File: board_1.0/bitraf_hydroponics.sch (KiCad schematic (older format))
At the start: 39 parts, among them P1 12V_PWR, P10 LDR, P11 ROT_BTN, P12 SWITCH_2, P13 I2C_4, P14 I2C_3, P15 I2C_2, P16 I2C_1, P17 SWITCH_3, P2 BREAKOUT_1-15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

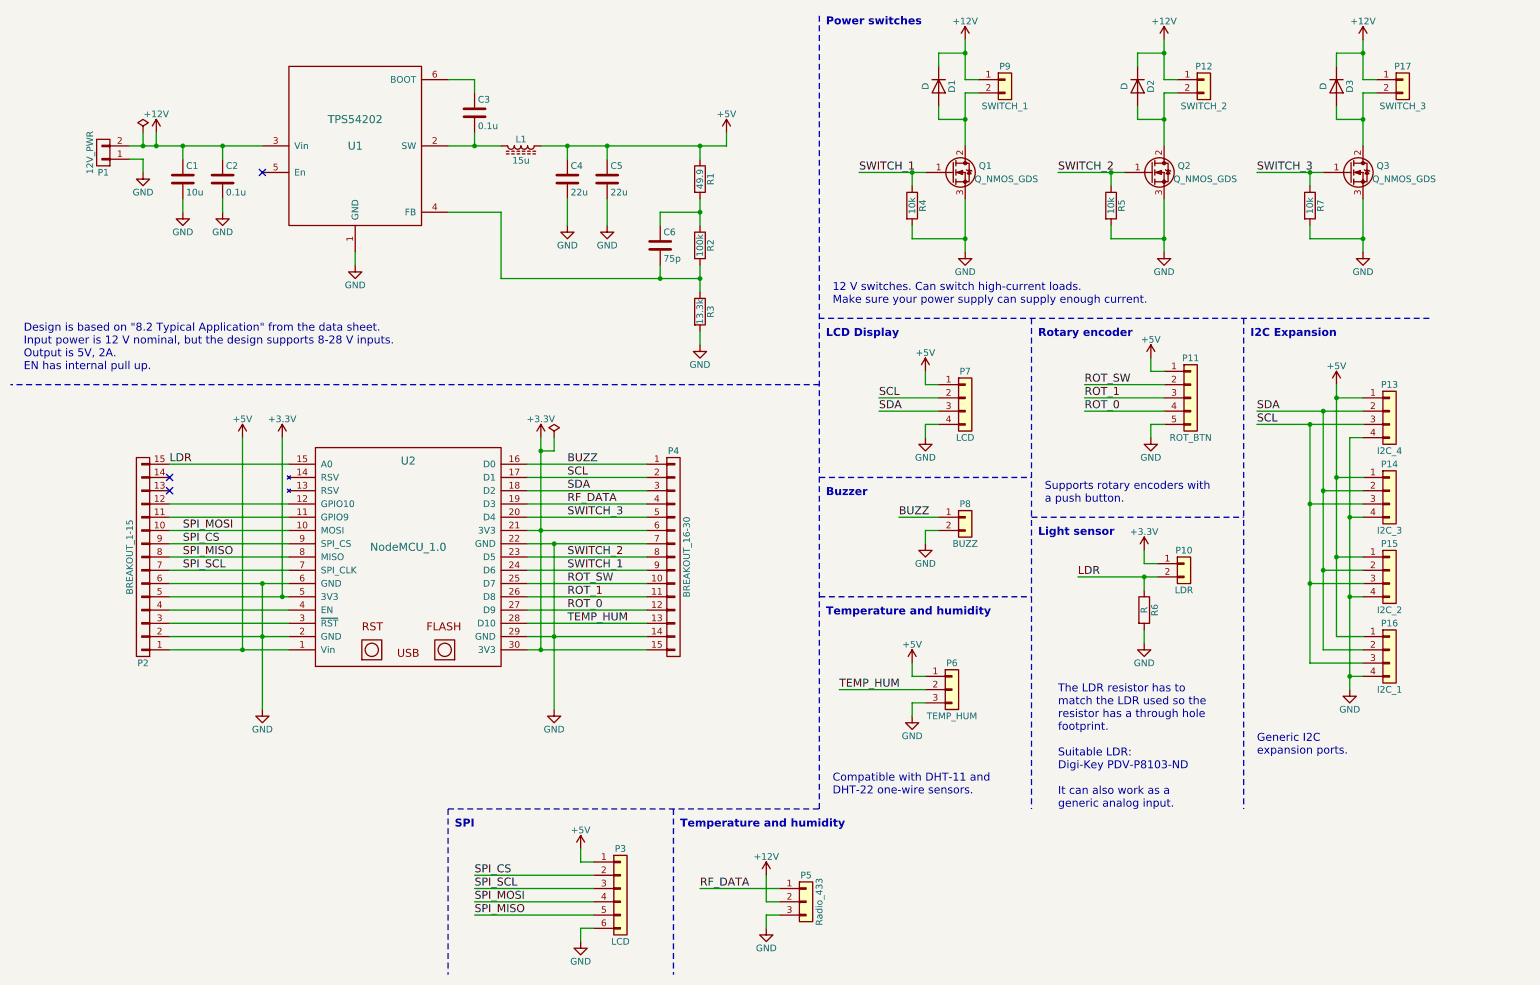
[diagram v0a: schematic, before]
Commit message: o Replacing NodeMCU with a single ESP-12F module and an LDO.   Will need an external programmer.
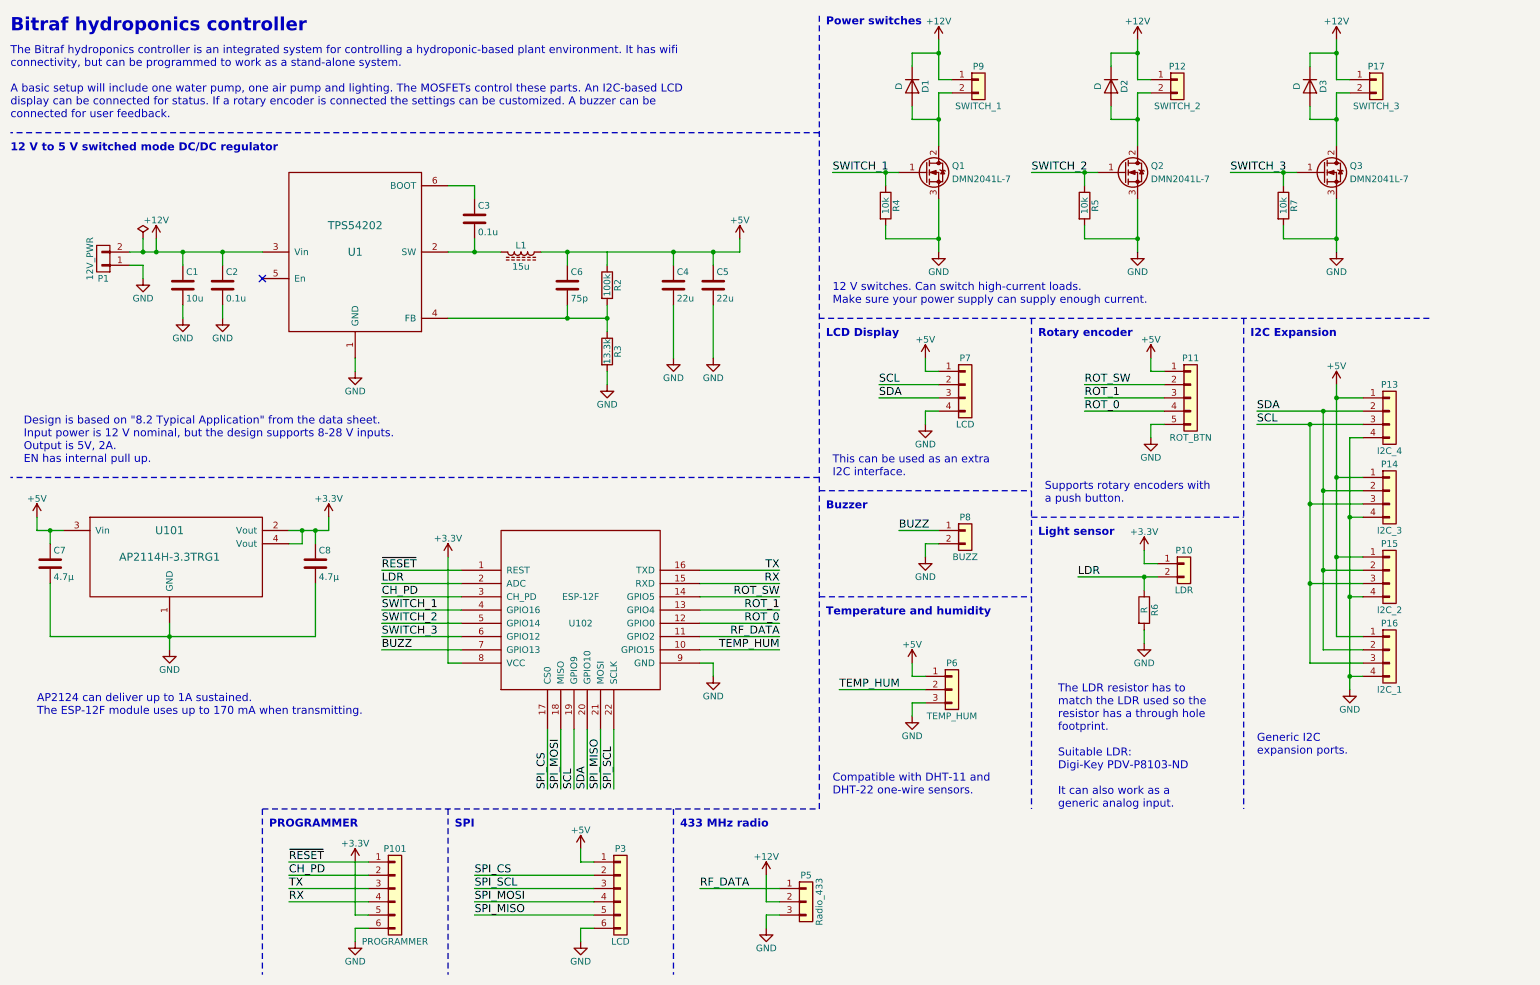
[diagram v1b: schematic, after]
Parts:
- removed P2: BREAKOUT_1-15, symbol CONN_01X15
- removed P4: BREAKOUT_16-30, symbol CONN_01X15
- removed R1: 49.9, symbol R
- removed U2: NodeMCU_1.0, symbol NodeMCU_1.0
- added C7, C8: 4.7µ, symbol C
- added P101: PROGRAMMER, symbol Conn_01x06
- added U101: AP2114H-3.3TRG1, TO_SOT_Packages_SMD:SOT-223, symbol AP2114H-3.3TRG1
- added U102: ESP-12F, ESP8266:ESP-12E, symbol ESP-12F
- Q1, Q2, Q3: value Q_NMOS_GDS -> DMN2041L-7
- U1: footprint (none) -> TO_SOT_Packages_SMD:SOT-23-6_Handsoldering
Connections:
- net +3V3: now also C8.1, P101.5 (Pin_5), U101.2 (Vout), U101.4 (Vout), U102.8 (VCC)
- net +5V: now also C6.1, C7.1, U101.3 (Vin)
- net BUZZ: now also U102.7 (GPIO13)
- net GND: now also C7.2, C8.2, P101.6 (Pin_6), U101.1 (GND), U102.9 (GND)
- net LDR: now also U102.2 (ADC)
- net RF_DATA: now also U102.11 (GPIO2)
- net ROT_0: now also U102.12 (GPIO0)
- net ROT_1: now also U102.13 (GPIO4)
- net ROT_SW: now also U102.14 (GPIO5)
- net SCL: now also U102.19 (GPIO9)
- net SDA: now also U102.20 (GPIO10)
- net SPI_CS: now also U102.17 (CS0)
- net SPI_MISO: now also U102.21 (MOSI)
- net SPI_MOSI: now also U102.18 (MISO)
- net SPI_SCL: now also U102.22 (SCLK)
- net SWITCH_1: now also U102.4 (GPIO16)
- net SWITCH_2: now also U102.5 (GPIO14)
- net SWITCH_3: now also U102.6 (GPIO12)
- net TEMP_HUM: now also U102.10 (GPIO15)
- net at R2.1: no longer C6.1
- new net CH_PD: P101.2 (Pin_2), U102.3 (CH_PD)
- new net RX: P101.4 (Pin_4), U102.15 (RXD)
- new net TX: P101.3 (Pin_3), U102.16 (TXD)
- new net ~RESET: P101.1 (Pin_1), U102.1 (REST)
- no-connect marks 3 -> 1
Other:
- note added: "12 V to 5 V switched mode DC/DC regulator"
- note added: "433 MHz radio"
- note added: "AP2124 can deliver up to 1A sustained.\nThe ESP-12F module uses up to 170 mA when transmitting."
- note added: "Bitraf hydroponics controller"
- note added: "PROGRAMMER"
- note added: "The Bitraf hydroponics controller is an integrated system for controlling a hydroponic-based plant environment. It has wifi\nconnectivity, but can be programmed to work as a stand-alone system.\n\nA basic setup will include one water pump, one air pump and lighting. The MOSFETs control these parts. An I2C-based LCD\ndisplay can be connected for status. If a rotary encoder is connected the setting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"
- note added: "This can be used as an extra\nI2C interface."
- moved on the sheet: C1, C2, C3, C4, C5, C6, D1, D2, D3, L1, P1, P12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

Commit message: o Selecting components for flyback diodes. o Adding footprints for MOSFETs. o More comments.
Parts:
- D1, D2, D3: value D -> S1MTR; footprint (none) -> Diodes_SMD:D_SMA_Handsoldering
- Q1, Q2, Q3: footprint (none) -> TO_SOT_Packages_SMD:SOT-23
- renumbered U101 to U2, U102 to U3
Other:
- note added: "Flyback diodes are "fast rectifier diodes" for inductive loads. DC Reverse Vr(max) is 1000 V,\nIo is 1 A. The MOSFETs have Vdss = 20 V, Rds(on) = 26 mΩ @ 3.3 V, Id = 6.4 A.\n"
- note removed: "12 V switches. Can switch high-current loads.\nMake sure your power supply can supply enough current."
- moved on the sheet: Q1, Q2, Q3, R4, R5, R7

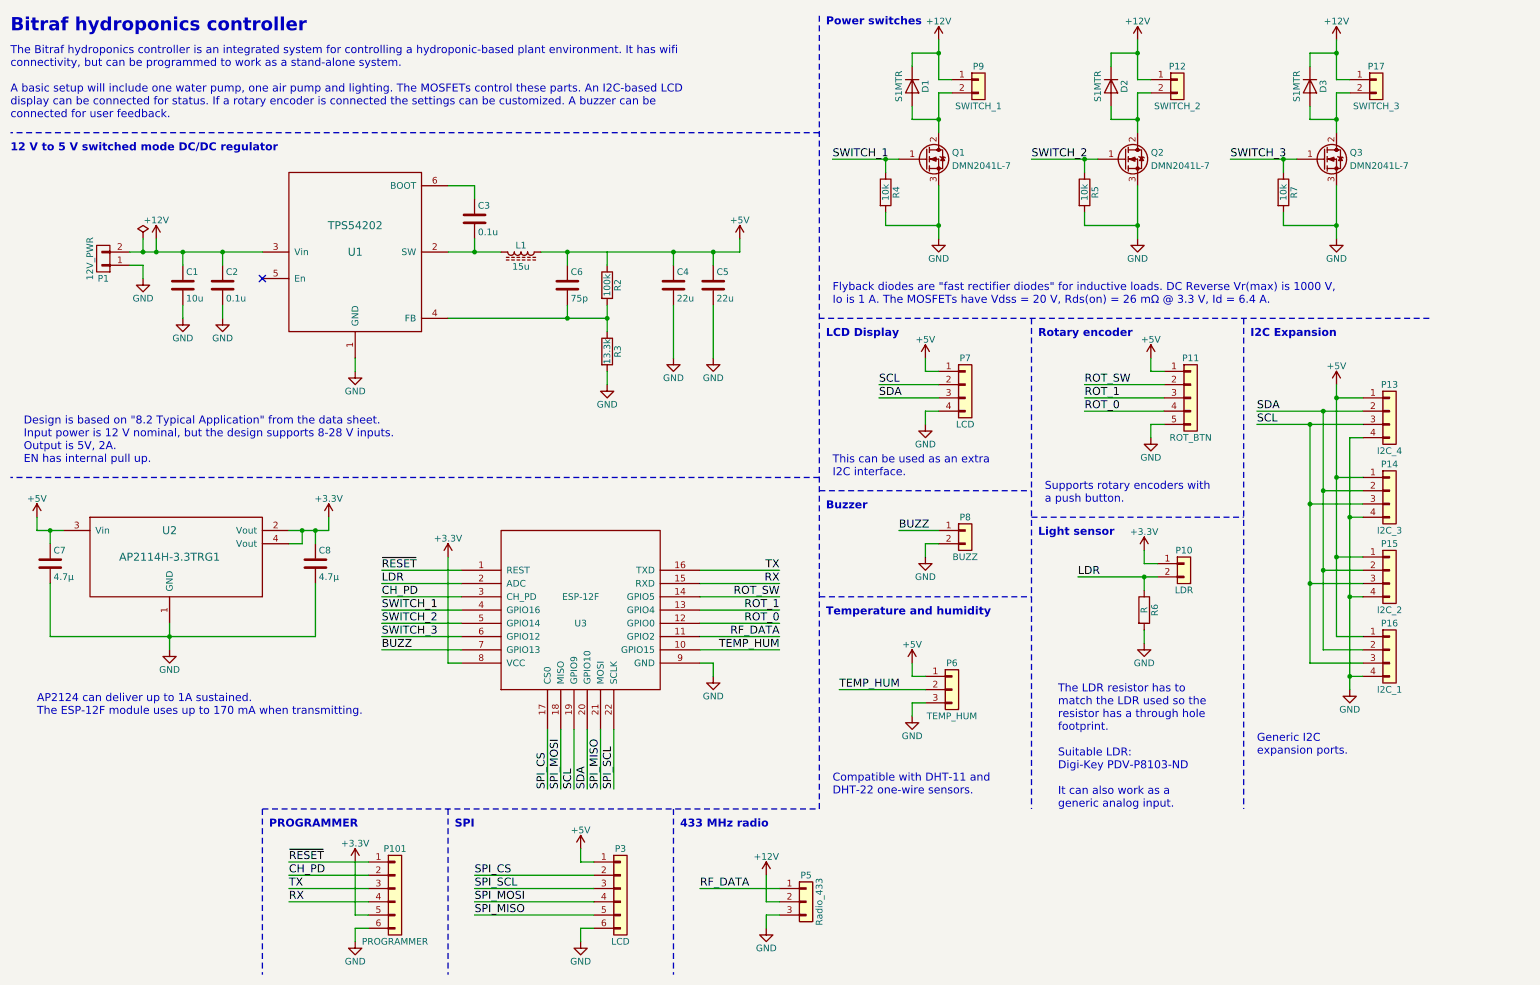
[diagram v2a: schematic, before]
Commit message: o Selecting the rest of the footprints. Using 0805 as default SMD size to make it makerspace friendly. o Some more nitpicking.
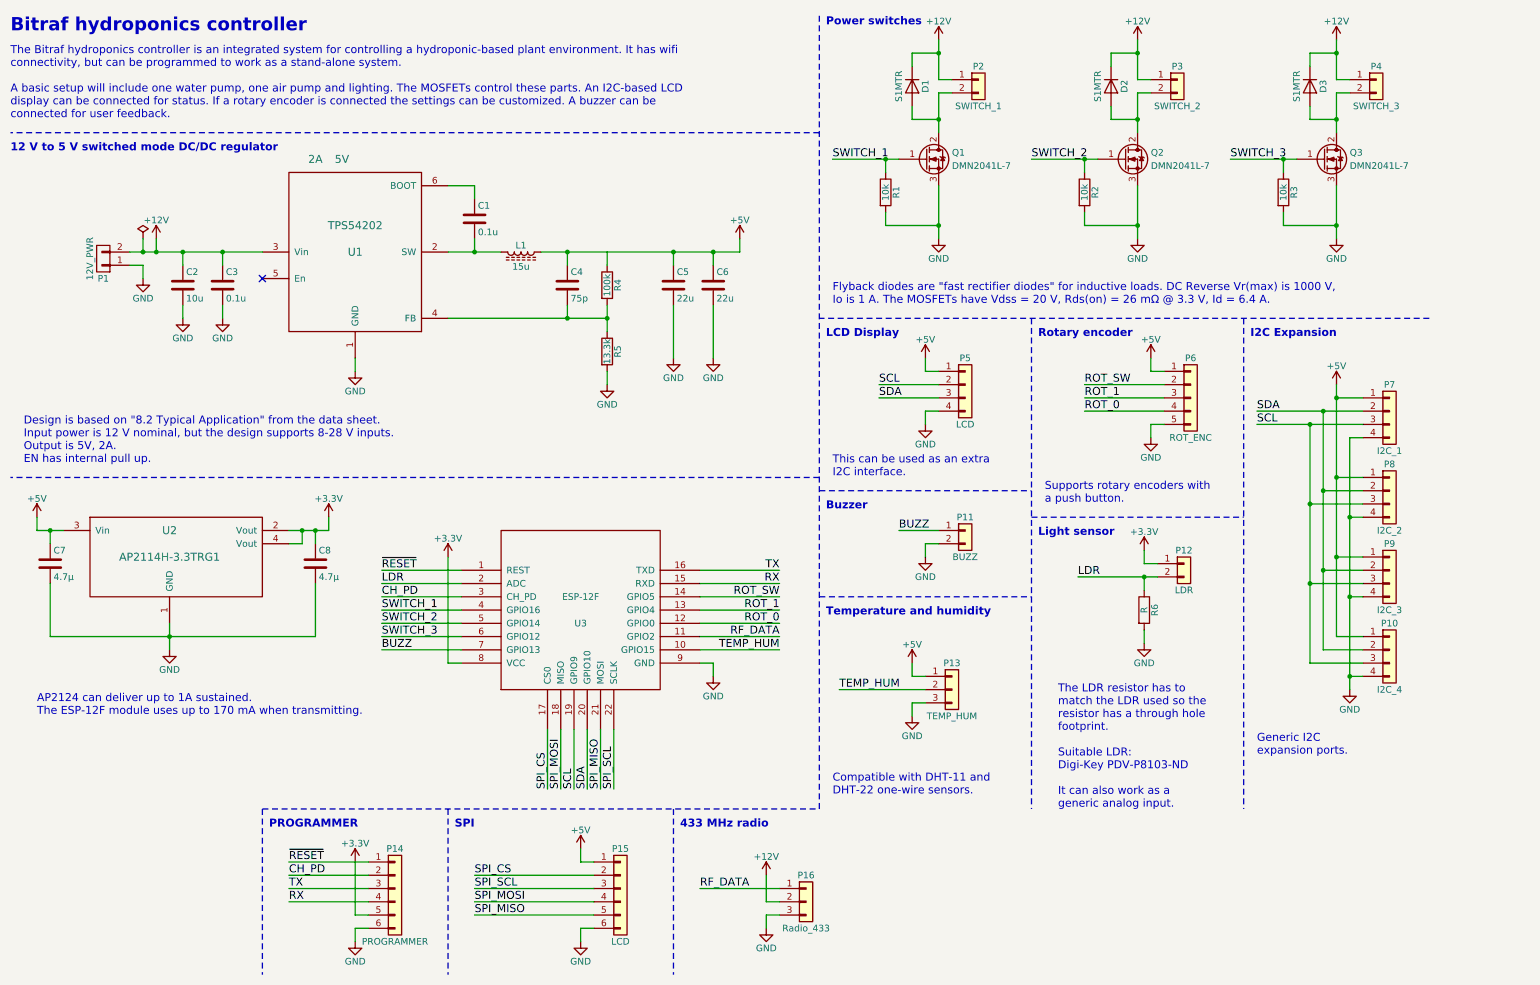
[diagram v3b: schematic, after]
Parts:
- C1: renamed from C3; footprint (none) -> Capacitors_SMD:C_0805
- C2: renamed from C1; footprint (none) -> Capacitors_SMD:C_0805
- C3: renamed from C2; footprint (none) -> Capacitors_SMD:C_0805
- C4: renamed from C6; footprint (none) -> Capacitors_SMD:C_0805
- C5: renamed from C4; footprint (none) -> Capacitors_SMD:C_0805
- C6: renamed from C5; footprint (none) -> Capacitors_SMD:C_0805
- C7, C8: footprint (none) -> Capacitors_SMD:C_0805
- L1: footprint (none) -> Inductors_SMD:L_Taiyo-Yuden_NR-80xx
- P1: footprint (none) -> Connectors_Terminal_Blocks:TerminalBlock_Pheonix_PT-3.5mm_2pol
- P10: renamed from P13; footprint (none) -> Pin_Headers:Pin_Header_Straight_1x04_Pitch2.54mm
- P11: renamed from P8; footprint (none) -> Connectors_Phoenix:PhoenixContact_PTSM0,5_4-HV-2,5_SMD
- P12: renamed from P10; footprint (none) -> Connectors_Phoenix:PhoenixContact_PTSM0,5_4-HV-2,5_SMD
- P13: renamed from P6; footprint (none) -> Pin_Headers:Pin_Header_Straight_1x03_Pitch2.54mm
- P14: renamed from P101; footprint (none) -> Pin_Headers:Pin_Header_Straight_1x06_Pitch2.54mm
- P15: renamed from P3; footprint (none) -> Pin_Headers:Pin_Header_Straight_1x06_Pitch2.54mm
- P16: renamed from P5; footprint (none) -> Socket_Strips:Socket_Strip_Straight_1x03_Pitch2.54mm
- P2: renamed from P9; footprint (none) -> Connectors_Phoenix:PhoenixContact_PTSM0,5_4-HV-2,5_SMD
- P3: renamed from P12; footprint (none) -> Connectors_Phoenix:PhoenixContact_PTSM0,5_4-HV-2,5_SMD
- P4: renamed from P17; footprint (none) -> Connectors_Phoenix:PhoenixContact_PTSM0,5_4-HV-2,5_SMD
- P5: renamed from P7; footprint (none) -> Pin_Headers:Pin_Header_Straight_1x04_Pitch2.54mm
- P6: renamed from P11; value ROT_BTN -> ROT_ENC; footprint (none) -> Pin_Headers:Pin_Header_Straight_1x05_Pitch2.54mm
- P7: renamed from P16; footprint (none) -> Pin_Headers:Pin_Header_Straight_1x04_Pitch2.54mm
- P8: renamed from P15; footprint (none) -> Pin_Headers:Pin_Header_Straight_1x04_Pitch2.54mm
- P9: renamed from P14; footprint (none) -> Pin_Headers:Pin_Header_Straight_1x04_Pitch2.54mm
- R1: renamed from R4; footprint (none) -> Resistors_SMD:R_0805
- R2: renamed from R5; footprint (none) -> Resistors_SMD:R_0805
- R3: renamed from R7; footprint (none) -> Resistors_SMD:R_0805
- R4: renamed from R2; footprint (none) -> Resistors_SMD:R_0805
- R5: renamed from R3; footprint (none) -> Resistors_SMD:R_0805
- R6: footprint (none) -> Resistors_SMD:R_0805
- U1: Iout (none) -> 2A; Vout (none) -> 5V; mpn TPS54202 -> TPS54202DDCT
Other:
- moved on the sheet: P10, P7, P8, P9
